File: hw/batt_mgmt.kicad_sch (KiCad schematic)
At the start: 1 part

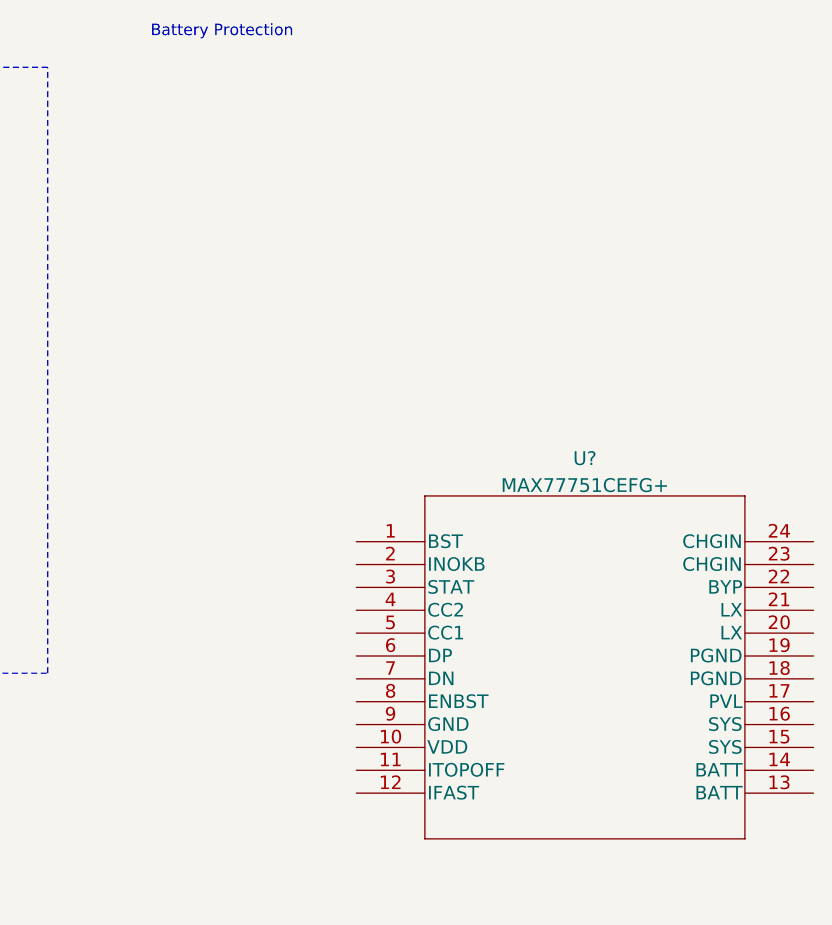
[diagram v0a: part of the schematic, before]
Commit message: MAX77751CEFG+ Symbol fix
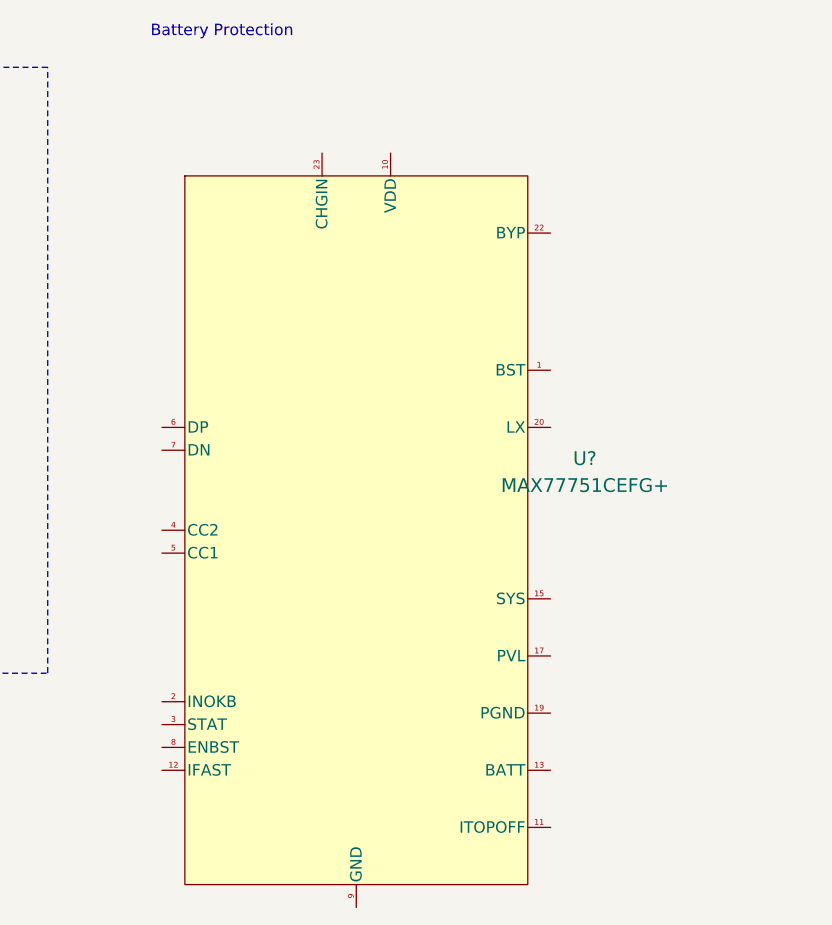
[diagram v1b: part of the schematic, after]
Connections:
- net at U?.13 (BATT): now also U?.14 (BATT)
- net at U?.15 (SYS): now also U?.16 (SYS)
- net PGND: now reaches U?.18 (PGND)
- net PGND: now also U?.19 (PGND)
- net at U?.20 (LX): now also U?.21 (LX)
- net at U?.23 (CHGIN): now also U?.24 (CHGIN)

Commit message: lolz
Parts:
- removed U?: MAX77751CEFG+, 21-100385_90-100128_MXM, symbol 1.Power.Battery_Management:MAX77751CEFG+
- added BT1: Batt, symbol Device:Battery_Cell
- added C10, C16: 10${uF}, Capacitor_Tantalum_SMD:CP_EIA-2012-15_AVX-P, symbol Device:C_Polarized_US
- added C11: 22${uF}, Capacitor_Tantalum_SMD:CP_EIA-2012-15_AVX-P, symbol Device:C_Polarized_US
- added C12, C13, C14, C15: 100nF, Capacitor_SMD:C_0201_0603Metric, symbol Device:C
- added C9: 2.2${uF}, Capacitor_SMD:C_0201_0603Metric, symbol Device:C
- added J2: USB_C_Receptacle, 0:USB_C_Receptacle_Amphenol_12401548E4-2A, symbol Connector:USB_C_Receptacle
- added L2: 0.47${uh}, 1.Inductors.L_SRN_LAB2:L_SRN_2016_2012-R47M, symbol 1.Inductors.L_SRN_LAB2:L_SRN_2016_2010-R47M
- added U5: MAX77751CEFG+, 1.Power.BattMgmt:MAX77751CEFG+, symbol 1.Power.BattMgmt:MAX77751CEFG+
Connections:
- new net: BT1.1 (+), C16.1, U5.13 (BATT), U5.14 (BATT)
- new net: C12.1, U5.1 (BST)
- new net: C9.1, U5.10 (VDD)
- new net: C13.1, U5.17 (PVL)
- new net: C12.2, L2.1, U5.20 (LX), U5.21 (LX)
- new net: C10.1, C11.1, U5.22 (BYP)
- new net: U5.23 (CHGIN), U5.24 (CHGIN)
- new net: J2.A1 (GND), J2.A12 (GND), J2.B1 (GND), J2.B12 (GND)
- new net: J2.A4 (VBUS), J2.A9 (VBUS), J2.B4 (VBUS), J2.B9 (VBUS)
- new net +5V: C14.1, C15.1, L2.2, U5.15 (SYS), U5.16 (SYS)
- new net GND: BT1.2 (-), C10.2, C11.2, C13.2, C14.2, C15.2, C16.2, C9.2, U5.18 (PGND), U5.19 (PGND), U5.9 (GND)
- new net INOK: U5.2 (INOKB)
- new net ITO: U5.11 (ITOPOFF)
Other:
- note removed: "Battery Charger"
- note removed: "Battery Monitor"
- note removed: "Battery Protection"
